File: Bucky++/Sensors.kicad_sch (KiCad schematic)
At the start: 25 parts, among them IC1 INA239AQDGSRQ1, IC2 INA239AQDGSRQ1, IC2001 INA239AQDGSRQ1, IC3 INA239AQDGSRQ1, IC6 INA239AQDGSRQ1

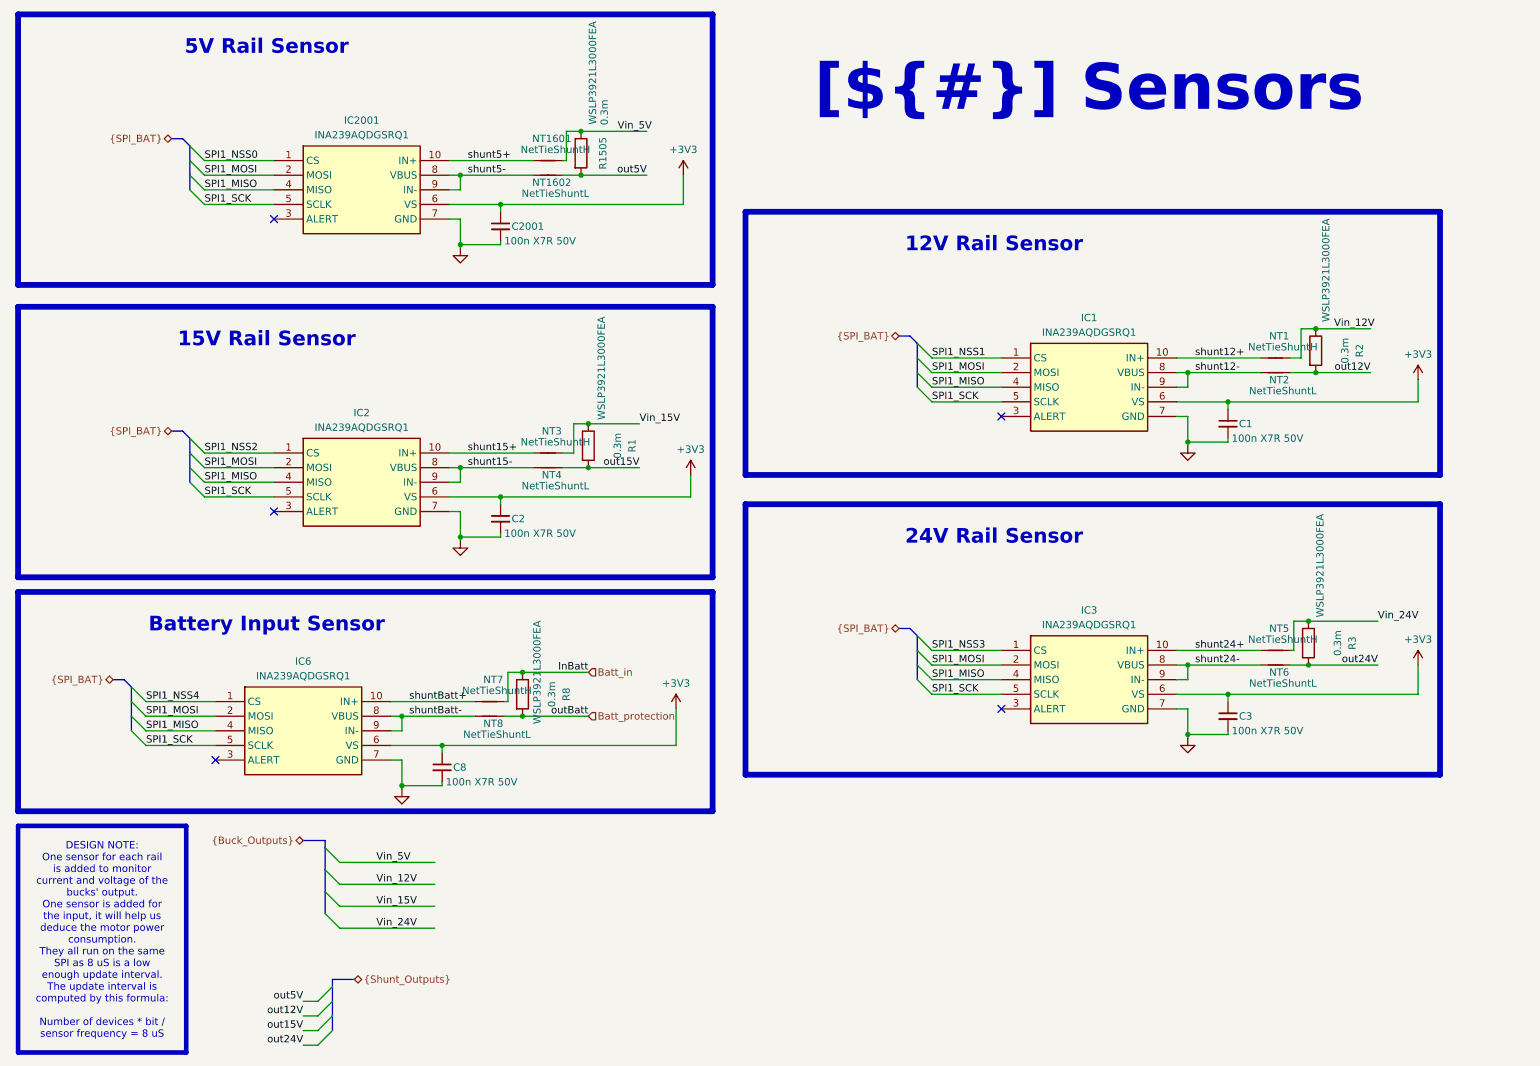
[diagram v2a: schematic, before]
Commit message: updated circuit after review. updated silkscreen
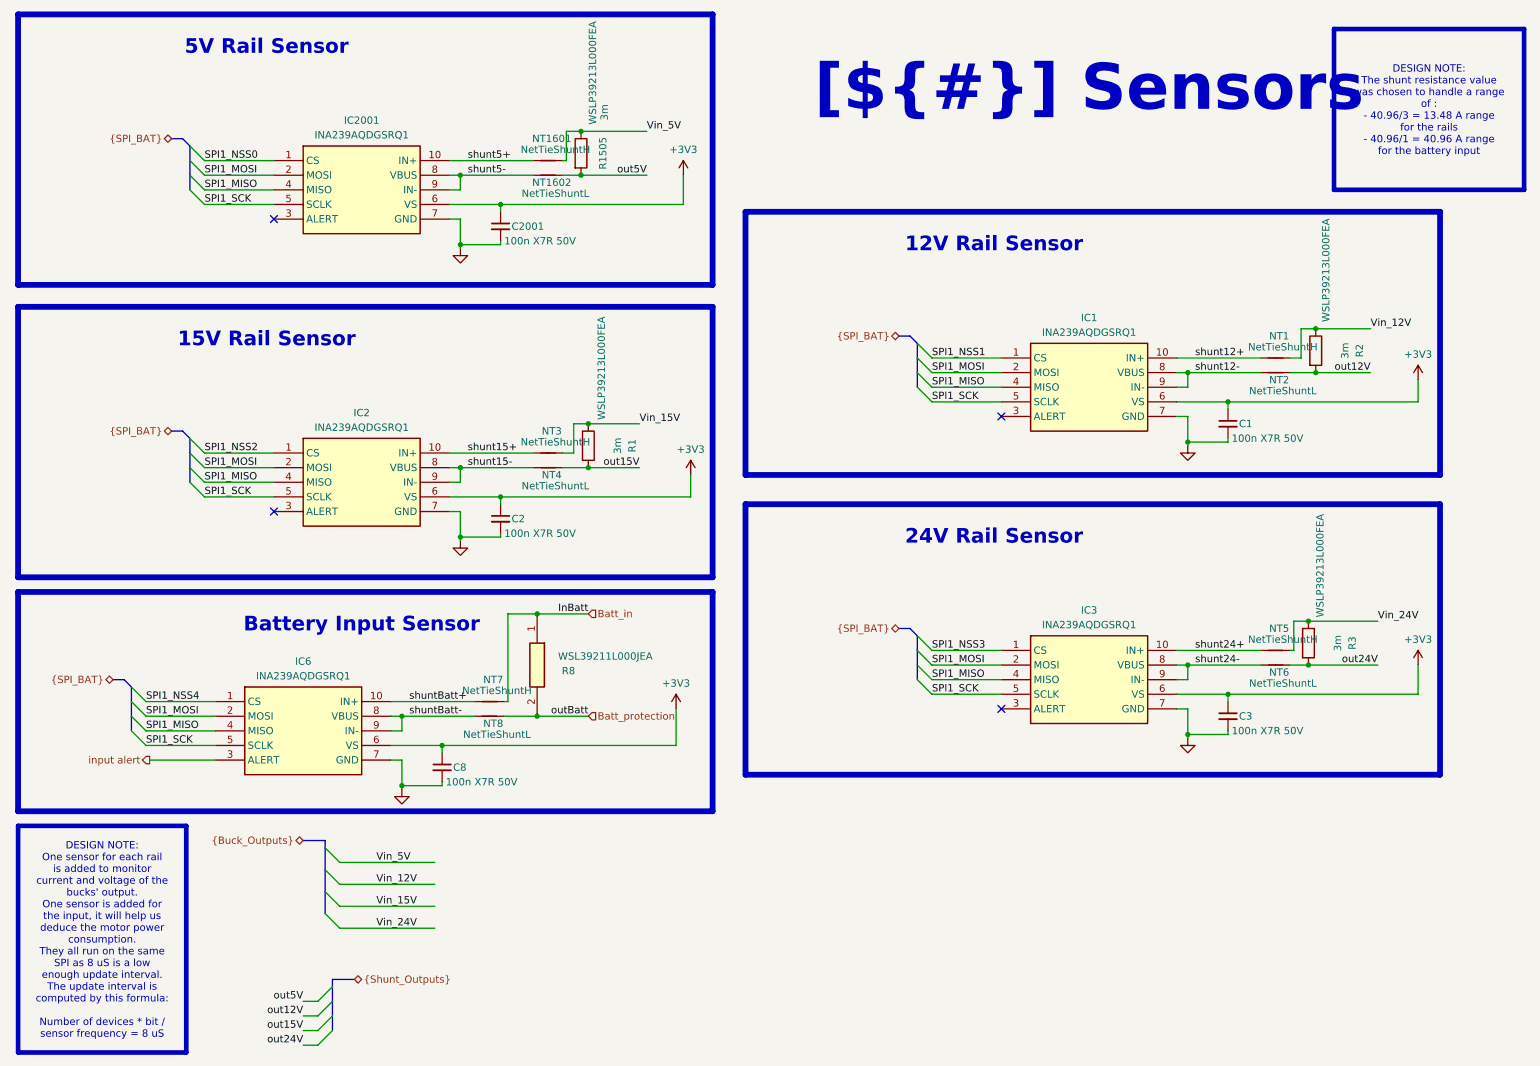
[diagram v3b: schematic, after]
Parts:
- removed R8: 0.3m, 0_resistor_smd:RES_WSLP3921_.003OHM_VIS, symbol Device:R
- added R8: WSL39211L000JEA, WSL39211L000JEA, symbol SamacSys_Parts:WSL39211L000JEA
- R1, R1505, R2, R3: value 0.3m -> 3m; Model WSLP3921L3000FEA -> WSLP39213L000FEA
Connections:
- net Batt_in: now also R8.1
- net Batt_protection: now also R8.2
- net input alert: now reaches IC6.3 (ALERT)
- no-connect marks 5 -> 4
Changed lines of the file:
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@@
 	(text_box "Battery Input Sensor\n"
 		(exclude_from_sim no)
-		(at 16.51 114.935 0)
-		(size 86.36 9.525)
+		(at 49.53 114.935 0)
+		(size 53.34 9.525)
 		(margins 1.9049 1.9049 1.9049 1.9049)
 		(stroke
@@
 		)
 	)
+	(text_box "DESIGN NOTE:\nThe shunt resistance value was chosen to handle a range of :\n- 40.96/3 = 13.48 A range for the rails\n- 40.96/1 = 40.96 A range for the battery input\n"
+		(exclude_from_sim no)
+		(at 245.11 17.78 0)
+		(size 33.02 27.94)
+		(margins 1.3525 1.3525 1.3525 1.3525)
+		(stroke
+			(width 0.8)
+			(type solid)
+			(color 200 200 200 1)
+		)
+		(fill
+			(type none)
+		)
+		(effects
+			(font
+				(face "Arial")
+				(size 1.27 1.27)
+				(color 0 0 0 1)
+			)
+		)
+	)
 	(text_box "5V Rail Sensor\n"
 		(exclude_from_sim no)
@@
 	)
 	(junction
+		(at 106.68 119.38)
+		(diameter 0)
+		(color 0 0 0 0)
+	)
+	(junction
 		(at 240.665 120.65)
 		(diameter 0)
@@
 	)
 	(junction
-		(at 104.14 129.54)
-		(diameter 0)
-		(color 0 0 0 0)
-	)
-	(junction
-		(at 104.14 137.16)
-		(diameter 0)
-		(color 0 0 0 0)
-	)
-	(junction
 		(at 115.57 93.98)
 		(diameter 0)
@@
 	)
 	(junction
+		(at 106.68 137.16)
+		(diameter 0)
+		(color 0 0 0 0)
+	)
+	(junction
 		(at 219.71 89.535)
 		(diameter 0)
@@
 	)
 	(no_connect
-		(at 50.8 144.78)
-	)
-	(no_connect
 		(at 187.325 135.89)
 	)
@@
 	(wire
 		(pts
-			(xy 104.14 129.54) (xy 115.57 129.54)
+			(xy 101.6 119.38) (xy 106.68 119.38)
 		)
 		(stroke
@@
 	(wire
 		(pts
+			(xy 39.37 144.78) (xy 50.8 144.78)
+		)
+		(stroke
+			(width 0)
+			(type default)
+		)
+	)
+	(wire
+		(pts
 			(xy 81.28 142.24) (xy 90.17 142.24)
 		)
@@
 	(wire
 		(pts
-			(xy 101.6 129.54) (xy 104.14 129.54)
-		)
-		(stroke
-			(width 0)
-			(type default)
-		)
-	)
-	(wire
-		(pts
 			(xy 241.935 69.85) (xy 251.46 69.85)
 		)
@@
 	(wire
 		(pts
-			(xy 101.6 129.54) (xy 101.6 134.62)
+			(xy 101.6 119.38) (xy 101.6 134.62)
 		)
 		(stroke
@@
 		)
 	)
+	(wire
+		(pts
+			(xy 106.68 137.16) (xy 115.57 137.16)
+		)
+		(stroke
+			(width 0)
+			(type default)
+		)
+	)
 	(bus
 		(pts
@@
 		)
 	)
+	(wire
+		(pts
+			(xy 106.68 119.38) (xy 115.57 119.38)
+		)
+		(stroke
+			(width 0)
+			(type default)
+		)
+	)
 	(bus
 		(pts
@@
 	(wire
 		(pts
-			(xy 100.965 137.16) (xy 104.14 137.16)
-		)
-		(stroke
-			(width 0)
-			(type default)
-		)
-	)
-	(wire
-		(pts
 			(xy 113.03 91.44) (xy 111.125 91.44)
 		)
@@
 	(wire
 		(pts
-			(xy 104.14 137.16) (xy 115.57 137.16)
+			(xy 100.965 137.16) (xy 106.68 137.16)
 		)
 		(stroke
@@
 	)
 	(label "Vin_5V"
-		(at 120.65 35.56 0)
+		(at 125.73 35.56 0)
 		(effects
 			(font
@@
 	)
 	(label "Vin_12V"
-		(at 245.11 69.85 0)
+		(at 251.46 69.85 0)
 		(effects
 			(font
@@
 	)
 	(label "InBatt"
-		(at 115.57 129.54 180)
+		(at 115.57 119.38 180)
 		(effects
 			(font
@@
 		)
 	)
+	(hierarchical_label "input alert"
+		(shape output)
+		(at 39.37 144.78 180)
+		(effects
+			(font
+				(size 1.27 1.27)
+			)
+			(justify right)
+		)
+	)
 	(hierarchical_label "{Buck_Outputs}"
 		(shape tri_state)
@@
 	(hierarchical_label "Batt_in"
 		(shape input)
-		(at 115.57 129.54 0)
+		(at 115.57 119.38 0)
 		(effects
 			(font
@@
 			)
 		)
-		(property "Value" "0.3m"
+		(property "Value" "3m"
 			(at 120.65 90.17 90)
 			(effects
@@
 			)
 		)
-		(property "Model" "WSLP3921L3000FEA"
+		(property "Model" "WSLP39213L000FEA"
 			(at 117.856 76.708 90)
 			(effects
@@
 	)
 	(symbol
-		(lib_name "R_1")
-		(lib_id "Device:R")
-		(at 104.14 133.35 0)
-		(unit 1)
-		(exclude_from_sim no)
-		(in_bom yes)
-		(on_board yes)
-		(dnp no)
-		(property "Reference" "R8"
-			(at 111.76 133.35 90)
-			(effects
-				(font
-					(size 1.27 1.27)
-				)
-			)
-		)
-		(property "Value" "0.3m"
-			(at 109.22 133.35 90)
-			(effects
-				(font
-					(size 1.27 1.27)
-				)
-			)
-		)
-		(property "Footprint" "0_resistor_smd:RES_WSLP3921_.003OHM_VIS"
-			(at 102.362 133.35 90)
-			(effects
-				(font
-					(size 1.27 1.27)
-				)
-				(hide yes)
-			)
-		)
-		(property "Datasheet" ""
-			(at 104.14 133.35 0)
-			(effects
-				(font
-					(size 1.27 1.27)
-				)
-				(hide yes)
-			)
-		)
-		(property "Description" ""
-			(at 104.14 133.35 0)
-			(effects
-				(font
-					(size 1.27 1.27)
-				)
-				(hide yes)
-			)
-		)
-		(property "Model" "WSLP3921L3000FEA"
-			(at 106.68 129.54 90)
-			(effects
-				(font
-					(size 1.27 1.27)
-				)
-			)
-		)
-		(pin "1"
-		)
-		(pin "2"
-		)
-		(instances
-			(project "Bucky++"
-				(path "/0650c7a8-acba-429c-9f8e-eec0baf0bc1c/fede4c36-00cc-4d3d-b71c-5243ba232202/0a3a8431-1070-4a1b-95bb-cb7cd1b8d37c"
-					(reference "R8")
-					(unit 1)
-				)
-			)
-		)
-	)
-	(symbol
 		(lib_id "Device:NetTie_2")
 		(at 108.585 93.98 0)
@@
 			)
 		)
-		(property "Value" "0.3m"
+		(property "Value" "3m"
 			(at 118.364 32.258 90)
 			(effects
@@
 			)
 		)
-		(property "Model" "WSLP3921L3000FEA"
+		(property "Model" "WSLP39213L000FEA"
 			(at 116.332 25.4 90)
 			(effects
@@
 			)
 		)
-		(property "Value" "0.3m"
+		(property "Value" "3m"
 			(at 245.745 124.46 90)
 			(effects
@@
 			)
 		)
-		(property "Model" "WSLP3921L3000FEA"
+		(property "Model" "WSLP39213L000FEA"
 			(at 242.697 110.998 90)
 			(effects
@@
 	)
 	(symbol
+		(lib_id "SamacSys_Parts:WSL39211L000JEA")
+		(at 106.68 119.38 270)
+		(unit 1)
+		(exclude_from_sim no)
+		(in_bom yes)
+		(on_board yes)
+		(dnp no)
+		(property "Reference" "R8"
+			(at 113.284 129.286 90)
+			(effects
+				(font
+					(size 1.27 1.27)
+				)
+				(justify right)
+			)
+		)
+		(property "Value" "WSL39211L000JEA"
+			(at 126.746 126.746 90)
+			(effects
+				(font
+					(size 1.27 1.27)
+				)
+				(justify right)
+			)
+		)
+		(property "Footprint" "WSL39211L000JEA"
+			(at 10.49 133.35 0)
+			(effects
+				(font
+					(size 1.27 1.27)
+				)
+				(justify left top)
+				(hide yes)
+			)
+		)
+		(property "Datasheet" "https://www.vishay.com/docs/30110/wsl3921-wsl5931.pdf"
+			(at -89.51 133.35 0)
+			(effects
+				(font
+					(size 1.27 1.27)
+				)
+				(justify left top)
+				(hide yes)
+			)
+		)
+		(property "Description" "1 mOhms +/-5% 3W Chip Resistor Nonstandard Anti-Sulfur, Automotive AEC-Q200, Current Sense, Moisture Resistant, Pulse Withstanding Metal Element"
+			(at 106.68 119.38 0)
+			(effects
+				(font
+					(size 1.27 1.27)
+				)
+				(hide yes)
+			)
+		)
+		(property "Height" "0.5"
+			(at -289.51 133.35 0)
+			(effects
+				(font
+					(size 1.27 1.27)
+				)
+				(justify left top)
+				(hide yes)
+			)
+		)
+		(property "RS Part Number" ""
+			(at -389.51 133.35 0)
+			(effects
+				(font
+					(size 1.27 1.27)
+				)
+				(justify left top)
+				(hide yes)
+			)
+		)
+		(property "RS Price/Stock" ""
+			(at -489.51 133.35 0)
+			(effects
+				(font
+					(size 1.27 1.27)
+				)
+				(justify left top)
+				(hide yes)
+			)
+		)
+		(property "Manufacturer_Name" "Vishay"
+			(at -589.51 133.35 0)
+			(effects
+				(font
+					(size 1.27 1.27)
+				)
+				(justify left top)
+				(hide yes)
+			)
+		)
+		(property "Manufacturer_Part_Number" "WSL39211L000JEA"
+			(at -689.51 133.35 0)
+			(effects
+				(font
+					(size 1.27 1.27)
+				)
+				(justify left top)
+				(hide yes)
+			)
+		)
+		(property "Allied_Number" "71589971"
+			(at -789.51 133.35 0)
+			(effects
+				(font
+					(size 1.27 1.27)
+				)
+				(justify left top)
+				(hide yes)
+			)
+		)
+		(pin "1"
+		)
+		(pin "2"
+		)
+		(instances
+			(project "Bucky++"
+				(path "/0650c7a8-acba-429c-9f8e-eec0baf0bc1c/fede4c36-00cc-4d3d-b71c-5243ba232202/0a3a8431-1070-4a1b-95bb-cb7cd1b8d37c"
+					(reference "R8")
+					(unit 1)
+				)
+			)
+		)
+	)
+	(symbol
 		(lib_id "power:GND")
 		(at 219.71 90.17 0)
@@
 			)
 		)
-		(property "Value" "0.3m"
+		(property "Value" "3m"
 			(at 247.015 73.66 90)
 			(effects
@@
 			)
 		)
-		(property "Model" "WSLP3921L3000FEA"
+		(property "Model" "WSLP39213L000FEA"
 			(at 243.713 59.69 90)
 			(effects

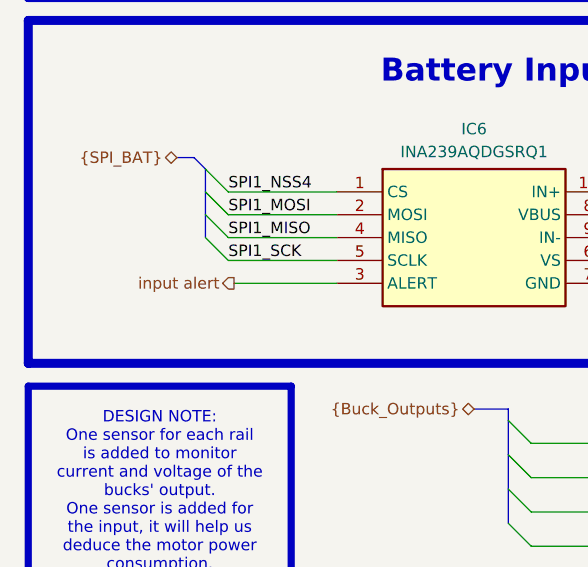
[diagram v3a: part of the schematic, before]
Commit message: fix layout and tolerance issues, started working on routing alerts
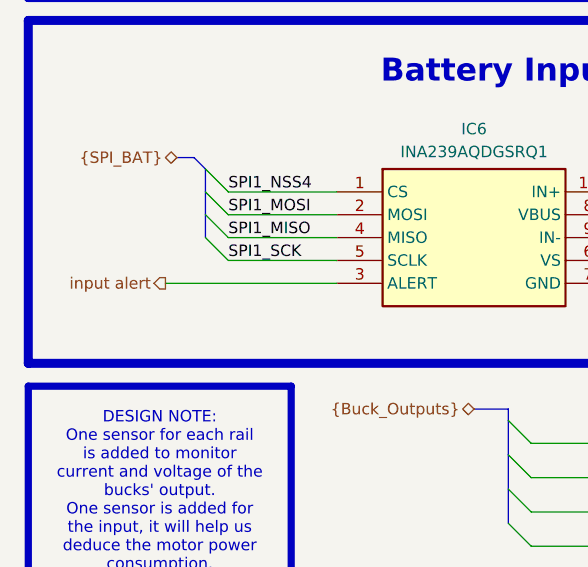
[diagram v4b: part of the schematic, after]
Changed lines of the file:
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@@
 	(wire
 		(pts
-			(xy 39.37 144.78) (xy 50.8 144.78)
+			(xy 31.75 144.78) (xy 50.8 144.78)
 		)
 		(stroke
@@
 	(hierarchical_label "input alert"
 		(shape output)
-		(at 39.37 144.78 180)
-		(effects
-			(font
+		(at 31.75 144.78 180)
+		(effects
+			(font
